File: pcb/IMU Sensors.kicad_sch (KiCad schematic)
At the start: 5 parts, among them U4 MS5607-02BA, U5 LSM6DSL

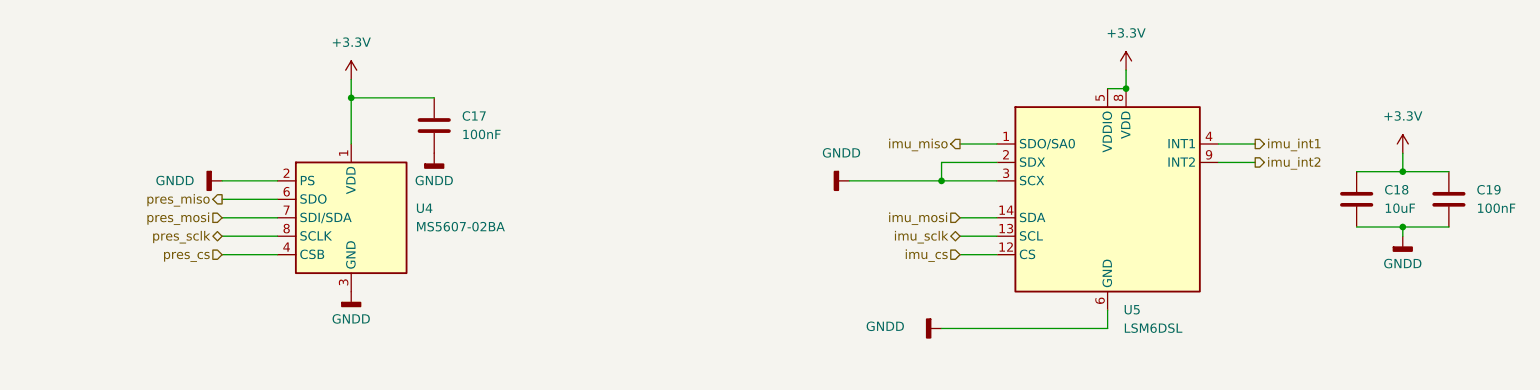
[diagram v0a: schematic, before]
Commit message: Added more testpoints
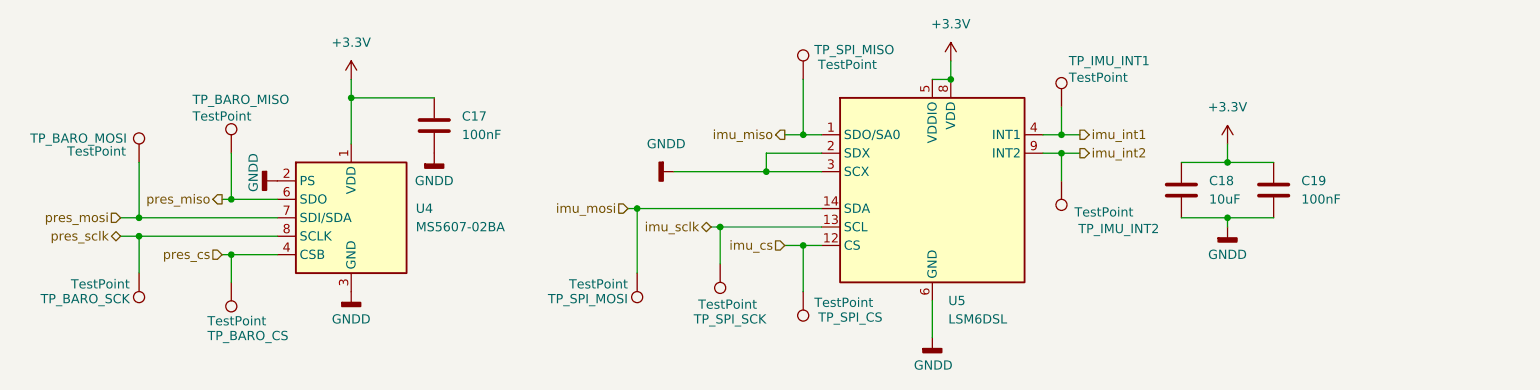
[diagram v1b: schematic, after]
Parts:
- added TP_BARO_CS, TP_BARO_MISO, TP_BARO_MOSI, TP_BARO_SCK, TP_IMU_INT1, TP_IMU_INT2, TP_SPI_CS, TP_SPI_MISO, TP_SPI_MOSI, TP_SPI_SCK: TestPoint, TestPoint:TestPoint_Loop_D2.54mm_Drill1.5mm_Beaded, symbol Connector:TestPoint
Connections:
- net imu_cs: now also TP_SPI_CS.1
- net imu_int1: now also TP_IMU_INT1.1
- net imu_int2: now also TP_IMU_INT2.1
- net imu_miso: now also TP_SPI_MISO.1
- net imu_mosi: now also TP_SPI_MOSI.1
- net imu_sclk: now also TP_SPI_SCK.1
- net pres_cs: now also TP_BARO_CS.1
- net pres_miso: now also TP_BARO_MISO.1
- net pres_mosi: now also TP_BARO_MOSI.1
- net pres_sclk: now also TP_BARO_SCK.1
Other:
- moved on the sheet: C18, C19, U5

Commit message: Updated Schematics
Completed Schematics for Test Bed, updated pcb
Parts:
- renumbered C17 to C15, C18 to C16, C19 to C17, TP_BARO_CS to TP_BARO_CS1, TP_BARO_MISO to TP_BARO_MISO1, TP_BARO_MOSI to TP_BARO_MOSI1, TP_BARO_SCK to TP_BARO_SCK1, TP_SPI_CS to TP_SPI_CS1, TP_SPI_MISO to TP_SPI_MISO1, TP_SPI_MOSI to TP_SPI_MOSI1, TP_SPI_SCK to TP_SPI_SCK1
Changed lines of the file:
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@@
 		(on_board yes)
 		(dnp no)
-		(property "Reference" "#PWR057"
+		(property "Reference" "#PWR064"
 			(at 62.23 95.25 0)
 			(effects
@@
 			(project "Sensors"
 				(path "/ba7b4294-8d75-4b9e-892f-fb52727887ec/7b15f5f2-9385-4263-9cd0-b3960b130352"
-					(reference "#PWR057")
+					(reference "#PWR064")
 					(unit 1)
 				)
@@
 		(dnp no)
 		(fields_autoplaced yes)
-		(property "Reference" "#PWR065"
+		(property "Reference" "#PWR072"
 			(at 199.39 107.95 0)
 			(effects
@@
 			(project "Sensors"
 				(path "/ba7b4294-8d75-4b9e-892f-fb52727887ec/7b15f5f2-9385-4263-9cd0-b3960b130352"
-					(reference "#PWR065")
+					(reference "#PWR072")
 					(unit 1)
 				)
@@
 		(on_board yes)
 		(dnp no)
-		(property "Reference" "TP_SPI_MOSI"
+		(property "Reference" "TP_SPI_MOSI1"
 			(at 116.84 111.506 0)
 			(effects
@@
 			(project "control-module"
 				(path "/ba7b4294-8d75-4b9e-892f-fb52727887ec/7b15f5f2-9385-4263-9cd0-b3960b130352"
-					(reference "TP_SPI_MOSI")
+					(reference "TP_SPI_MOSI1")
 					(unit 1)
 				)
@@
 		(on_board yes)
 		(dnp no)
-		(property "Reference" "TP_SPI_CS"
+		(property "Reference" "TP_SPI_CS1"
 			(at 151.892 114.046 0)
 			(effects
@@
 			(project "control-module"
 				(path "/ba7b4294-8d75-4b9e-892f-fb52727887ec/7b15f5f2-9385-4263-9cd0-b3960b130352"
-					(reference "TP_SPI_CS")
+					(reference "TP_SPI_CS1")
 					(unit 1)
 				)
@@
 		(on_board yes)
 		(dnp no)
-		(property "Reference" "TP_BARO_SCK"
+		(property "Reference" "TP_BARO_SCK1"
 			(at 48.26 111.506 0)
 			(effects
@@
 			(project "control-module"
 				(path "/ba7b4294-8d75-4b9e-892f-fb52727887ec/7b15f5f2-9385-4263-9cd0-b3960b130352"
-					(reference "TP_BARO_SCK")
+					(reference "TP_BARO_SCK1")
 					(unit 1)
 				)
@@
 		(dnp no)
 		(fields_autoplaced yes)
-		(property "Reference" "#PWR063"
+		(property "Reference" "#PWR070"
 			(at 161.29 82.55 0)
 			(effects
@@
 			(project "Sensors"
 				(path "/ba7b4294-8d75-4b9e-892f-fb52727887ec/7b15f5f2-9385-4263-9cd0-b3960b130352"
-					(reference "#PWR063")
+					(reference "#PWR070")
 					(unit 1)
 				)
@@
 		(dnp no)
 		(fields_autoplaced yes)
-		(property "Reference" "C17"
+		(property "Reference" "C15"
 			(at 93.98 86.3599 0)
 			(effects
@@
 			(project "Sensors"
 				(path "/ba7b4294-8d75-4b9e-892f-fb52727887ec/7b15f5f2-9385-4263-9cd0-b3960b130352"
-					(reference "C17")
+					(reference "C15")
 					(unit 1)
 				)
@@
 		(on_board yes)
 		(dnp no)
-		(property "Reference" "TP_BARO_CS"
+		(property "Reference" "TP_BARO_CS1"
 			(at 70.104 116.586 0)
 			(effects
@@
 			(project "control-module"
 				(path "/ba7b4294-8d75-4b9e-892f-fb52727887ec/7b15f5f2-9385-4263-9cd0-b3960b130352"
-					(reference "TP_BARO_CS")
+					(reference "TP_BARO_CS1")
 					(unit 1)
 				)
@@
 		(dnp no)
 		(fields_autoplaced yes)
-		(property "Reference" "#PWR061"
+		(property "Reference" "#PWR068"
 			(at 116.84 93.98 0)
 			(effects
@@
 			(project "Sensors"
 				(path "/ba7b4294-8d75-4b9e-892f-fb52727887ec/7b15f5f2-9385-4263-9cd0-b3960b130352"
-					(reference "#PWR061")
+					(reference "#PWR068")
 					(unit 1)
 				)
@@
 		(on_board yes)
 		(dnp no)
-		(property "Reference" "#PWR062"
+		(property "Reference" "#PWR069"
 			(at 158.75 123.19 0)
 			(effects
@@
 			(project "Sensors"
 				(path "/ba7b4294-8d75-4b9e-892f-fb52727887ec/7b15f5f2-9385-4263-9cd0-b3960b130352"
-					(reference "#PWR062")
+					(reference "#PWR069")
 					(unit 1)
 				)
@@
 		(dnp no)
 		(fields_autoplaced yes)
-		(property "Reference" "#PWR058"
+		(property "Reference" "#PWR065"
 			(at 78.74 85.09 0)
 			(effects
@@
 			(project "Sensors"
 				(path "/ba7b4294-8d75-4b9e-892f-fb52727887ec/7b15f5f2-9385-4263-9cd0-b3960b130352"
-					(reference "#PWR058")
+					(reference "#PWR065")
 					(unit 1)
 				)
@@
 		(dnp no)
 		(fields_autoplaced yes)
-		(property "Reference" "#PWR059"
+		(property "Reference" "#PWR066"
 			(at 78.74 116.84 0)
 			(effects
@@
 			(project "Sensors"
 				(path "/ba7b4294-8d75-4b9e-892f-fb52727887ec/7b15f5f2-9385-4263-9cd0-b3960b130352"
-					(reference "#PWR059")
+					(reference "#PWR066")
 					(unit 1)
 				)
@@
 		(dnp no)
 		(fields_autoplaced yes)
-		(property "Reference" "#PWR060"
+		(property "Reference" "#PWR067"
 			(at 90.17 97.79 0)
 			(effects
@@
 			(project "Sensors"
 				(path "/ba7b4294-8d75-4b9e-892f-fb52727887ec/7b15f5f2-9385-4263-9cd0-b3960b130352"
-					(reference "#PWR060")
+					(reference "#PWR067")
 					(unit 1)
 				)
@@
 		(on_board yes)
 		(dnp no)
-		(property "Reference" "TP_BARO_MISO"
+		(property "Reference" "TP_BARO_MISO1"
 			(at 56.896 84.074 0)
 			(effects
@@
 			(project "control-module"
 				(path "/ba7b4294-8d75-4b9e-892f-fb52727887ec/7b15f5f2-9385-4263-9cd0-b3960b130352"
-					(reference "TP_BARO_MISO")
+					(reference "TP_BARO_MISO1")
 					(unit 1)
 				)
@@
 		(on_board yes)
 		(dnp no)
-		(property "Reference" "TP_SPI_MISO"
+		(property "Reference" "TP_SPI_MISO1"
 			(at 142.494 77.216 0)
 			(effects
@@
 			(project "control-module"
 				(path "/ba7b4294-8d75-4b9e-892f-fb52727887ec/7b15f5f2-9385-4263-9cd0-b3960b130352"
-					(reference "TP_SPI_MISO")
+					(reference "TP_SPI_MISO1")
 					(unit 1)
 				)
@@
 		(dnp no)
 		(fields_autoplaced yes)
-		(property "Reference" "C19"
+		(property "Reference" "C17"
 			(at 209.55 95.2499 0)
 			(effects
@@
 			(project "Sensors"
 				(path "/ba7b4294-8d75-4b9e-892f-fb52727887ec/7b15f5f2-9385-4263-9cd0-b3960b130352"
-					(reference "C19")
+					(reference "C17")
 					(unit 1)
 				)
@@
 		(on_board yes)
 		(dnp no)
-		(property "Reference" "TP_BARO_MOSI"
+		(property "Reference" "TP_BARO_MOSI1"
 			(at 34.544 89.408 0)
 			(effects
@@
 			(project "control-module"
 				(path "/ba7b4294-8d75-4b9e-892f-fb52727887ec/7b15f5f2-9385-4263-9cd0-b3960b130352"
-					(reference "TP_BARO_MOSI")
+					(reference "TP_BARO_MOSI1")
 					(unit 1)
 				)
@@
 		(dnp no)
 		(fields_autoplaced yes)
-		(property "Reference" "#PWR064"
+		(property "Reference" "#PWR071"
 			(at 199.39 93.98 0)
 			(effects
@@
 			(project "Sensors"
 				(path "/ba7b4294-8d75-4b9e-892f-fb52727887ec/7b15f5f2-9385-4263-9cd0-b3960b130352"
-					(reference "#PWR064")
+					(reference "#PWR071")
 					(unit 1)
 				)
@@
 		(on_board yes)
 		(dnp no)
-		(property "Reference" "TP_SPI_SCK"
+		(property "Reference" "TP_SPI_SCK1"
 			(at 135.89 114.3 0)
 			(effects
@@
 			(project "control-module"
 				(path "/ba7b4294-8d75-4b9e-892f-fb52727887ec/7b15f5f2-9385-4263-9cd0-b3960b130352"
-					(reference "TP_SPI_SCK")
+					(reference "TP_SPI_SCK1")
 					(unit 1)
 				)
@@
 		(dnp no)
 		(fields_autoplaced yes)
-		(property "Reference" "C18"
+		(property "Reference" "C16"
 			(at 196.85 95.2499 0)
 			(effects
@@
 			(project "Sensors"
 				(path "/ba7b4294-8d75-4b9e-892f-fb52727887ec/7b15f5f2-9385-4263-9cd0-b3960b130352"
-					(reference "C18")
-					(unit 1)
-				)
+					(reference "C16")
+					(unit 1)
+				)

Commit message: Pre-fab update
Pre fab update
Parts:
- renumbered TP_BARO_CS1 to BARO_CS1, TP_BARO_MISO1 to BARO_MISO1, TP_BARO_MOSI1 to BARO_MOSI1, TP_BARO_SCK1 to BARO_SCK1, TP_IMU_INT1 to IMU_INT1, TP_IMU_INT2 to IMU_INT2, TP_SPI_CS1 to SPI_CS1, TP_SPI_MISO1 to SPI_MISO1, TP_SPI_MOSI1 to SPI_MOSI1, TP_SPI_SCK1 to SPI_SCK1
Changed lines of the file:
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@@
 		(on_board yes)
 		(dnp no)
-		(property "Reference" "TP_IMU_INT1"
+		(property "Reference" "IMU_INT1"
 			(at 177.546 78.74 0)
 			(effects
@@
 			)
 		)
+		(property "Sim.Device" ""
+			(at 176.53 85.09 0)
+			(effects
+				(font
+					(size 1.27 1.27)
+				)
+				(hide yes)
+			)
+		)
 		(pin "1"
 		)
@@
 			(project "control-module"
 				(path "/ba7b4294-8d75-4b9e-892f-fb52727887ec/7b15f5f2-9385-4263-9cd0-b3960b130352"
-					(reference "TP_IMU_INT1")
+					(reference "IMU_INT1")
 					(unit 1)
 				)
@@
 		(on_board yes)
 		(dnp no)
-		(property "Reference" "TP_SPI_MOSI1"
+		(property "Reference" "SPI_MOSI1"
 			(at 116.84 111.506 0)
 			(effects
@@
 			)
 		)
+		(property "Sim.Device" ""
+			(at 118.11 107.95 0)
+			(effects
+				(font
+					(size 1.27 1.27)
+				)
+				(hide yes)
+			)
+		)
 		(pin "1"
 		)
@@
 			(project "control-module"
 				(path "/ba7b4294-8d75-4b9e-892f-fb52727887ec/7b15f5f2-9385-4263-9cd0-b3960b130352"
-					(reference "TP_SPI_MOSI1")
+					(reference "SPI_MOSI1")
 					(unit 1)
 				)
@@
 		(on_board yes)
 		(dnp no)
-		(property "Reference" "TP_SPI_CS1"
+		(property "Reference" "SPI_CS1"
 			(at 151.892 114.046 0)
 			(effects
@@
 			)
 		)
+		(property "Sim.Device" ""
+			(at 140.97 110.49 0)
+			(effects
+				(font
+					(size 1.27 1.27)
+				)
+				(hide yes)
+			)
+		)
 		(pin "1"
 		)
@@
 			(project "control-module"
 				(path "/ba7b4294-8d75-4b9e-892f-fb52727887ec/7b15f5f2-9385-4263-9cd0-b3960b130352"
-					(reference "TP_SPI_CS1")
+					(reference "SPI_CS1")
 					(unit 1)
 				)
@@
 		(on_board yes)
 		(dnp no)
-		(property "Reference" "TP_BARO_SCK1"
+		(property "Reference" "BARO_SCK1"
 			(at 48.26 111.506 0)
 			(effects
@@
 			)
 		)
+		(property "Sim.Device" ""
+			(at 49.53 107.95 0)
+			(effects
+				(font
+					(size 1.27 1.27)
+				)
+				(hide yes)
+			)
+		)
 		(pin "1"
 		)
@@
 			(project "control-module"
 				(path "/ba7b4294-8d75-4b9e-892f-fb52727887ec/7b15f5f2-9385-4263-9cd0-b3960b130352"
-					(reference "TP_BARO_SCK1")
+					(reference "BARO_SCK1")
 					(unit 1)
 				)
@@
 			)
 		)
+		(property "Sim.Device" ""
+			(at 90.17 87.63 0)
+			(effects
+				(font
+					(size 1.27 1.27)
+				)
+				(hide yes)
+			)
+		)
 		(pin "2"
 		)
@@
 			)
 		)
+		(property "Sim.Device" ""
+			(at 78.74 100.33 0)
+			(effects
+				(font
+					(size 1.27 1.27)
+				)
+				(hide yes)
+			)
+		)
 		(pin "8"
 		)
@@
 		(on_board yes)
 		(dnp no)
-		(property "Reference" "TP_BARO_CS1"
+		(property "Reference" "BARO_CS1"
 			(at 70.104 116.586 0)
 			(effects
@@
 			)
 		)
+		(property "Sim.Device" ""
+			(at 62.23 109.22 0)
+			(effects
+				(font
+					(size 1.27 1.27)
+				)
+				(hide yes)
+			)
+		)
 		(pin "1"
 		)
@@
 			(project "control-module"
 				(path "/ba7b4294-8d75-4b9e-892f-fb52727887ec/7b15f5f2-9385-4263-9cd0-b3960b130352"
-					(reference "TP_BARO_CS1")
+					(reference "BARO_CS1")
 					(unit 1)
 				)
@@
 		(on_board yes)
 		(dnp no)
-		(property "Reference" "TP_BARO_MISO1"
+		(property "Reference" "BARO_MISO1"
 			(at 56.896 84.074 0)
 			(effects
@@
 			)
 		)
+		(property "Sim.Device" ""
+			(at 62.23 91.44 0)
+			(effects
+				(font
+					(size 1.27 1.27)
+				)
+				(hide yes)
+			)
+		)
 		(pin "1"
 		)
@@
 			(project "control-module"
 				(path "/ba7b4294-8d75-4b9e-892f-fb52727887ec/7b15f5f2-9385-4263-9cd0-b3960b130352"
-					(reference "TP_BARO_MISO1")
+					(reference "BARO_MISO1")
 					(unit 1)
 				)
@@
 		(on_board yes)
 		(dnp no)
-		(property "Reference" "TP_SPI_MISO1"
+		(property "Reference" "SPI_MISO1"
 			(at 142.494 77.216 0)
 			(effects
@@
 			)
 		)
+		(property "Sim.Device" ""
+			(at 140.97 81.28 0)
+			(effects
+				(font
+					(size 1.27 1.27)
+				)
+				(hide yes)
+			)
+		)
 		(pin "1"
 		)
@@
 			(project "control-module"
 				(path "/ba7b4294-8d75-4b9e-892f-fb52727887ec/7b15f5f2-9385-4263-9cd0-b3960b130352"
-					(reference "TP_SPI_MISO1")
+					(reference "SPI_MISO1")
 					(unit 1)
 				)
@@
 			)
 		)
+		(property "Sim.Device" ""
+			(at 205.74 96.52 0)
+			(effects
+				(font
+					(size 1.27 1.27)
+				)
+				(hide yes)
+			)
+		)
 		(pin "2"
 		)
@@
 		(on_board yes)
 		(dnp no)
-		(property "Reference" "TP_BARO_MOSI1"
+		(property "Reference" "BARO_MOSI1"
 			(at 34.544 89.408 0)
 			(effects
@@
 			)
 		)
+		(property "Sim.Device" ""
+			(at 49.53 92.71 0)
+			(effects
+				(font
+					(size 1.27 1.27)
+				)
+				(hide yes)
+			)
+		)
 		(pin "1"
 		)
@@
 			(project "control-module"
 				(path "/ba7b4294-8d75-4b9e-892f-fb52727887ec/7b15f5f2-9385-4263-9cd0-b3960b130352"
-					(reference "TP_BARO_MOSI1")
+					(reference "BARO_MOSI1")
 					(unit 1)
 				)
@@
 			)
 		)
+		(property "Sim.Device" ""
+			(at 158.75 96.52 0)
+			(effects
+				(font
+					(size 1.27 1.27)
+				)
+				(hide yes)
+			)
+		)
 		(pin "4"
 		)
@@
 		(on_board yes)
 		(dnp no)
-		(property "Reference" "TP_SPI_SCK1"
+		(property "Reference" "SPI_SCK1"
 			(at 135.89 114.3 0)
 			(effects
@@
 			)
 		)
+		(property "Sim.Device" ""
+			(at 129.54 106.68 0)
+			(effects
+				(font
+					(size 1.27 1.27)
+				)
+				(hide yes)
+			)
+		)
 		(pin "1"
 		)
@@
 			(project "control-module"
 				(path "/ba7b4294-8d75-4b9e-892f-fb52727887ec/7b15f5f2-9385-4263-9cd0-b3960b130352"
-					(reference "TP_SPI_SCK1")
+					(reference "SPI_SCK1")
 					(unit 1)
 				)
@@
 		(on_board yes)
 		(dnp no)
-		(property "Reference" "TP_IMU_INT2"
+		(property "Reference" "IMU_INT2"
 			(at 189.992 101.854 0)
 			(effects
@@
 			)
 		)
+		(property "Sim.Device" ""
+			(at 176.53 95.25 0)
+			(effects
+				(font
+					(size 1.27 1.27)
+				)
+				(hide yes)
+			)
+		)
 		(pin "1"
 		)
@@
 			(project "control-module"
 				(path "/ba7b4294-8d75-4b9e-892f-fb52727887ec/7b15f5f2-9385-4263-9cd0-b3960b130352"
-					(reference "TP_IMU_INT2")
+					(reference "IMU_INT2")
 					(unit 1)
 				)
@@
 			)
 		)
+		(property "Sim.Device" ""
+			(at 193.04 96.52 0)
+			(effects
+				(font
+					(size 1.27 1.27)
+				)
+				(hide yes)
+			)
+		)

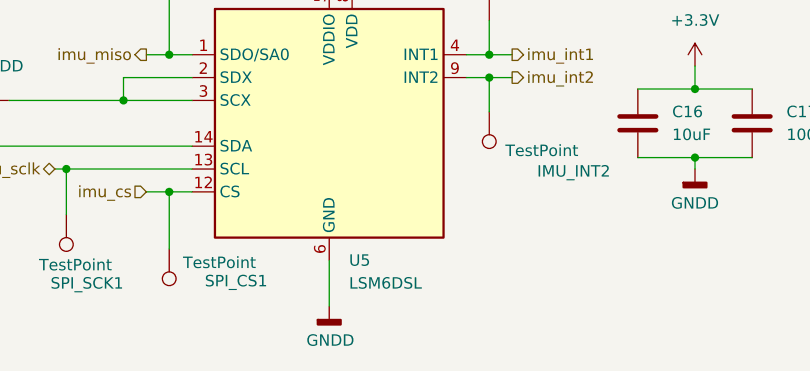
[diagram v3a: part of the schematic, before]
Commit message: Updated Schematics
R19 value updated to proper 220 Ohms
U5 value updated to new LSM6DSRTR
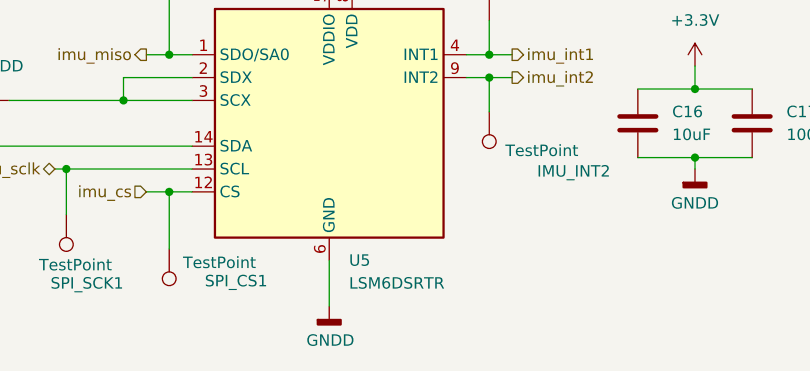
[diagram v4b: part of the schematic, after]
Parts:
- U5: value LSM6DSL -> LSM6DSRTR
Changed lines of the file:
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@@
 			)
 		)
-		(property "Value" "LSM6DSL"
+		(property "Value" "LSM6DSRTR"
 			(at 160.9441 114.3 0)
 			(effects
